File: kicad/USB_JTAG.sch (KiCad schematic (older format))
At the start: 19 parts, among them J1 USB_B, U4 NFM18PS, U5 WE-TVS-824011, U6 FT2232D, U7 6MHz_Crystal, U8 AT93C46DN-SH

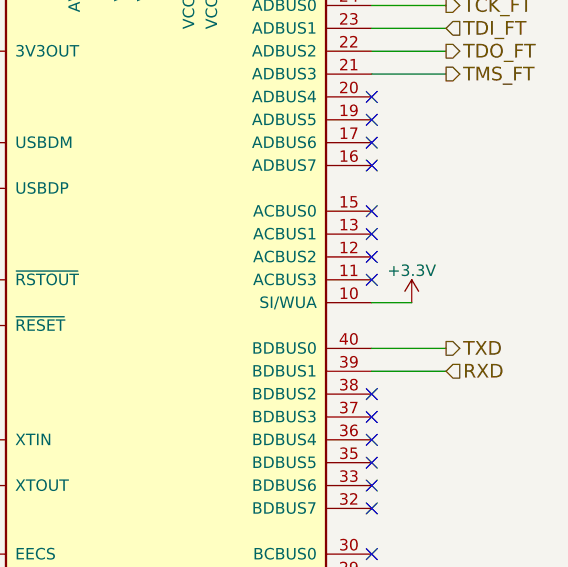
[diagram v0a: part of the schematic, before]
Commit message: Small layout and schematic changes
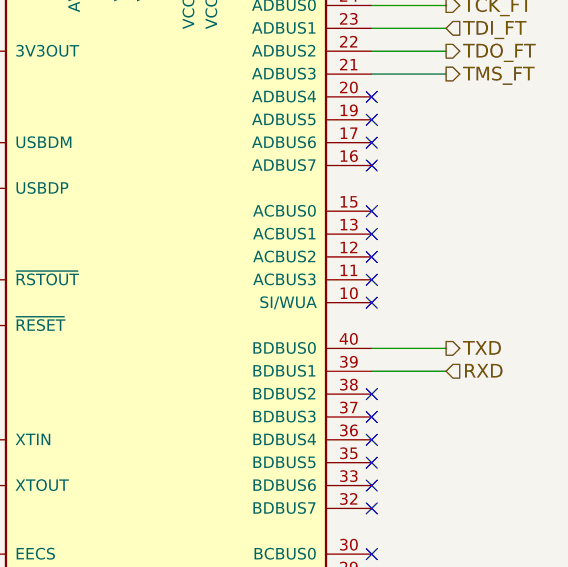
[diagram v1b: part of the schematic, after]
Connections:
- net +3V3: no longer U6.10 (SI/WUA)
- no-connect marks 21 -> 22
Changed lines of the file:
@@
 EESchema Schematic File Version 2
+LIBS:FrequnecyCounter-rescue
 LIBS:power
 LIBS:device
@@
 	1    0    0    -1
 $EndComp
-Wire Wire Line
-	7175 3525 7350 3525
-$Comp
-L +3.3V #PWR044
-U 1 1 59BBED1D
-P 7350 3525
-F 0 "#PWR044" H 7350 3375 50  0001 C CNN
-F 1 "+3.3V" H 7350 3665 50  0000 C CNN
-F 2 "" H 7350 3525 50  0001 C CNN
-F 3 "" H 7350 3525 50  0001 C CNN
-	1    7350 3525
-	1    0    0    -1
-$EndComp
 NoConn ~ 7175 4825
 NoConn ~ 7175 4925
@@
 	1    0    0    -1
 $EndComp
+NoConn ~ 7175 3525
 $EndSCHEMATC

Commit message: Small schematic and layout changes
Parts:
- added Q1: BC846B, TO_SOT_Packages_SMD:SOT-23, symbol BC846B
- added R12: 1k, Resistors_SMD:R_0603_HandSoldering, symbol R
- added R13: 150k, Resistors_SMD:R_0603_HandSoldering, symbol R
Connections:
- net +3V3: now also U6.10 (SI/WUA), U8.6 (ORG), U8.8 (VCC), R12.2
- net +5V: now also U6.4 (~RESET)
- net GND: now also U8.5 (GND), Q1.2 (E)
- net ~RESET: now also Q1.3 (C), R12.1; no longer U6.4 (~RESET)
- net at U6.41 (~PWREN): now also R13.2
- new net: Q1.1 (B), R13.1
- no-connect marks 22 -> 20
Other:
- moved on the sheet: C42
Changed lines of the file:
@@
 $EndComp
 $Comp
-L GND #PWR027
+L GND #PWR025
 U 1 1 595D2BC3
 P 1400 3350
-F 0 "#PWR027" H 1400 3100 50  0001 C CNN
+F 0 "#PWR025" H 1400 3100 50  0001 C CNN
 F 1 "GND" H 1400 3200 50  0000 C CNN
 F 2 "" H 1400 3350 50  0001 C CNN
@@
 $EndComp
 $Comp
-L GND #PWR028
+L GND #PWR026
 U 1 1 595D2BF4
 P 5975 5550
-F 0 "#PWR028" H 5975 5300 50  0001 C CNN
+F 0 "#PWR026" H 5975 5300 50  0001 C CNN
 F 1 "GND" H 5975 5400 50  0000 C CNN
 F 2 "" H 5975 5550 50  0001 C CNN
@@
 $EndComp
 $Comp
-L GND #PWR029
+L GND #PWR027
 U 1 1 595D2BFA
 P 5375 5025
-F 0 "#PWR029" H 5375 4775 50  0001 C CNN
+F 0 "#PWR027" H 5375 4775 50  0001 C CNN
 F 1 "GND" H 5375 4875 50  0000 C CNN
 F 2 "" H 5375 5025 50  0001 C CNN
@@
 $EndComp
 $Comp
-L GND #PWR030
+L GND #PWR028
 U 1 1 595D2C07
 P 5075 2425
-F 0 "#PWR030" H 5075 2175 50  0001 C CNN
+F 0 "#PWR028" H 5075 2175 50  0001 C CNN
 F 1 "GND" H 5075 2275 50  0000 C CNN
 F 2 "" H 5075 2425 50  0001 C CNN
@@
 $EndComp
 $Comp
-L GND #PWR031
+L GND #PWR029
 U 1 1 595D2C1A
 P 5450 2025
-F 0 "#PWR031" H 5450 1775 50  0001 C CNN
+F 0 "#PWR029" H 5450 1775 50  0001 C CNN
 F 1 "GND" H 5450 1875 50  0000 C CNN
 F 2 "" H 5450 2025 50  0001 C CNN
@@
 NoConn ~ 7175 4625
 NoConn ~ 7175 4725
-NoConn ~ 7175 5225
 $Comp
 L AT93C46DN-SH U8
@@
 $EndComp
 $Comp
-L +3.3V #PWR032
+L +3.3V #PWR030
 U 1 1 595E0732
 P 6375 1825
-F 0 "#PWR032" H 6375 1675 50  0001 C CNN
+F 0 "#PWR030" H 6375 1675 50  0001 C CNN
 F 1 "+3.3V" H 6375 1965 50  0000 C CNN
 F 2 "" H 6375 1825 50  0001 C CNN
@@
 $EndComp
 $Comp
-L GND #PWR033
+L GND #PWR031
 U 1 1 595E26E9
 P 2800 2450
-F 0 "#PWR033" H 2800 2200 50  0001 C CNN
+F 0 "#PWR031" H 2800 2200 50  0001 C CNN
 F 1 "GND" H 2800 2300 50  0000 C CNN
 F 2 "" H 2800 2450 50  0001 C CNN
@@
 $EndComp
 $Comp
-L GND #PWR034
+L GND #PWR032
 U 1 1 595E2C1D
 P 2075 3400
-F 0 "#PWR034" H 2075 3150 50  0001 C CNN
+F 0 "#PWR032" H 2075 3150 50  0001 C CNN
 F 1 "GND" H 2075 3250 50  0000 C CNN
 F 2 "" H 2075 3400 50  0001 C CNN
@@
 $EndComp
 $Comp
-L GND #PWR035
+L GND #PWR033
 U 1 1 595E6BEC
 P 2200 2250
-F 0 "#PWR035" H 2200 2000 50  0001 C CNN
+F 0 "#PWR033" H 2200 2000 50  0001 C CNN
 F 1 "GND" H 2200 2100 50  0000 C CNN
 F 2 "" H 2200 2250 50  0001 C CNN
@@
 	1    0    0    -1
 $EndComp
-NoConn ~ 3025 4900
 $Comp
 L C C39
@@
 $EndComp
 $Comp
-L GND #PWR036
+L GND #PWR034
 U 1 1 5961A2DE
 P 2400 3400
-F 0 "#PWR036" H 2400 3150 50  0001 C CNN
+F 0 "#PWR034" H 2400 3150 50  0001 C CNN
 F 1 "GND" H 2400 3250 50  0000 C CNN
 F 2 "" H 2400 3400 50  0001 C CNN
@@
 Text HLabel 7500 2525 2    60   Output ~ 0
 TMS_FT
-Text HLabel 5050 3625 0    60   Input ~ 0
-~RESET
-$Comp
-L +3.3V #PWR037
+$Comp
+L +3.3V #PWR035
 U 1 1 5964E324
 P 3850 4225
-F 0 "#PWR037" H 3850 4075 50  0001 C CNN
+F 0 "#PWR035" H 3850 4075 50  0001 C CNN
 F 1 "+3.3V" H 3850 4365 50  0000 C CNN
 F 2 "" H 3850 4225 50  0001 C CNN
@@
 $EndComp
 $Comp
-L +3.3V #PWR038
+L +3.3V #PWR036
 U 1 1 5964E7A5
-P 2750 4650
-F 0 "#PWR038" H 2750 4500 50  0001 C CNN
-F 1 "+3.3V" H 2750 4790 50  0000 C CNN
-F 2 "" H 2750 4650 50  0001 C CNN
-F 3 "" H 2750 4650 50  0001 C CNN
-	1    2750 4650
+P 2750 4625
+F 0 "#PWR036" H 2750 4475 50  0001 C CNN
+F 1 "+3.3V" H 2750 4765 50  0000 C CNN
+F 2 "" H 2750 4625 50  0001 C CNN
+F 3 "" H 2750 4625 50  0001 C CNN
+	1    2750 4625
 	1    0    0    -1
 $EndComp
@@
 L C C42
 U 1 1 5964E7E9
-P 2750 4800
-F 0 "C42" H 2775 4900 50  0000 L CNN
-F 1 "100n" H 2775 4700 50  0000 L CNN
-F 2 "Capacitors_SMD:C_0603_HandSoldering" H 2788 4650 50  0001 C CNN
-F 3 "" H 2750 4800 50  0001 C CNN
-	1    2750 4800
-	1    0    0    -1
-$EndComp
-$Comp
-L GND #PWR039
+P 2750 4775
+F 0 "C42" H 2775 4875 50  0000 L CNN
+F 1 "100n" H 2775 4675 50  0000 L CNN
+F 2 "Capacitors_SMD:C_0603_HandSoldering" H 2788 4625 50  0001 C CNN
+F 3 "" H 2750 4775 50  0001 C CNN
+	1    2750 4775
+	1    0    0    -1
+$EndComp
+$Comp
+L GND #PWR037
 U 1 1 5964E8AB
-P 2750 4950
-F 0 "#PWR039" H 2750 4700 50  0001 C CNN
-F 1 "GND" H 2750 4800 50  0000 C CNN
-F 2 "" H 2750 4950 50  0001 C CNN
-F 3 "" H 2750 4950 50  0001 C CNN
-	1    2750 4950
-	1    0    0    -1
-$EndComp
-$Comp
-L +5V #PWR040
+P 2750 4925
+F 0 "#PWR037" H 2750 4675 50  0001 C CNN
+F 1 "GND" H 2750 4775 50  0000 C CNN
+F 2 "" H 2750 4925 50  0001 C CNN
+F 3 "" H 2750 4925 50  0001 C CNN
+	1    2750 4925
+	1    0    0    -1
+$EndComp
+$Comp
+L +5V #PWR038
 U 1 1 5968BBC0
 P 2075 1925
-F 0 "#PWR040" H 2075 1775 50  0001 C CNN
+F 0 "#PWR038" H 2075 1775 50  0001 C CNN
 F 1 "+5V" H 2075 2065 50  0000 C CNN
 F 2 "" H 2075 1925 50  0001 C CNN
@@
 $EndComp
 $Comp
-L +5V #PWR041
+L +5V #PWR039
 U 1 1 596B00B1
 P 6125 1700
-F 0 "#PWR041" H 6125 1550 50  0001 C CNN
+F 0 "#PWR039" H 6125 1550 50  0001 C CNN
 F 1 "+5V" H 6125 1840 50  0000 C CNN
 F 2 "" H 6125 1700 50  0001 C CNN
@@
 $EndComp
 $Comp
-L +5V #PWR042
+L +5V #PWR040
 U 1 1 596CAD7A
 P 4950 1675
-F 0 "#PWR042" H 4950 1525 50  0001 C CNN
+F 0 "#PWR040" H 4950 1525 50  0001 C CNN
 F 1 "+5V" H 4950 1815 50  0000 C CNN
 F 2 "" H 4950 1675 50  0001 C CNN
@@
 	6075 1700 6175 1700
 Wire Wire Line
-	2750 4650 3025 4650
+	2750 4625 3025 4625
 Wire Wire Line
 	5375 3625 5050 3625
@@
 Connection ~ 4550 4325
 $Comp
-L GND #PWR043
+L GND #PWR041
 U 1 1 5973DDBE
 P 4550 4350
-F 0 "#PWR043" H 4550 4100 50  0001 C CNN
+F 0 "#PWR041" H 4550 4100 50  0001 C CNN
 F 1 "GND" H 4550 4200 50  0000 C CNN
 F 2 "" H 4550 4350 50  0001 C CNN
@@
 	7175 5025 7300 5025
 $Comp
-L +3.3V #PWR045
+L +3.3V #PWR042
 U 1 1 59C1476A
 P 7300 5025
-F 0 "#PWR045" H 7300 4875 50  0001 C CNN
+F 0 "#PWR042" H 7300 4875 50  0001 C CNN
 F 1 "+3.3V" H 7300 5165 50  0000 C CNN
 F 2 "" H 7300 5025 50  0001 C CNN
@@
 	1    0    0    -1
 $EndComp
-NoConn ~ 7175 3525
+$Comp
+L +5V #PWR043
+U 1 1 59FCA280
+P 5050 3625
+F 0 "#PWR043" H 5050 3475 50  0001 C CNN
+F 1 "+5V" H 5050 3765 50  0000 C CNN
+F 2 "" H 5050 3625 50  0001 C CNN
+F 3 "" H 5050 3625 50  0001 C CNN
+	1    5050 3625
+	1    0    0    -1
+$EndComp
+Wire Wire Line
+	7175 3525 7300 3525
+$Comp
+L +3.3V #PWR044
+U 1 1 59FCF531
+P 7300 3525
+F 0 "#PWR044" H 7300 3375 50  0001 C CNN
+F 1 "+3.3V" H 7300 3665 50  0000 C CNN
+F 2 "" H 7300 3525 50  0001 C CNN
+F 3 "" H 7300 3525 50  0001 C CNN
+	1    7300 3525
+	1    0    0    -1
+$EndComp
+$Comp
+L BC846B Q1
+U 1 1 59FD002C
+P 8100 5225
+F 0 "Q1" H 8300 5300 50  0000 L CNN
+F 1 "BC846B" H 8300 5225 50  0000 L CNN
+F 2 "TO_SOT_Packages_SMD:SOT-23" H 8300 5150 50  0001 L CIN
+F 3 "" H 8100 5225 50  0001 L CNN
+	1    8100 5225
+	1    0    0    -1
+$EndComp
+Wire Wire Line
+	7175 5225 7450 5225
+$Comp
+L R R13
+U 1 1 59FD0390
+P 7600 5225
+F 0 "R13" V 7680 5225 50  0000 C CNN
+F 1 "150k" V 7600 5225 50  0000 C CNN
+F 2 "Resistors_SMD:R_0603_HandSoldering" V 7530 5225 50  0001 C CNN
+F 3 "" H 7600 5225 50  0001 C CNN
+	1    7600 5225
+	0    1    1    0
+$EndComp
+Wire Wire Line
+	7750 5225 7900 5225
+$Comp
+L GND #PWR045
+U 1 1 59FD0919
+P 8200 5475
+F 0 "#PWR045" H 8200 5225 50  0001 C CNN
+F 1 "GND" H 8200 5325 50  0000 C CNN
+F 2 "" H 8200 5475 50  0001 C CNN
+F 3 "" H 8200 5475 50  0001 C CNN
+	1    8200 5475
+	1    0    0    -1
+$EndComp
+Wire Wire Line
+	8200 5475 8200 5425
+$Comp
+L R R12
+U 1 1 59FD09EE
+P 8200 4825
+F 0 "R12" V 8280 4825 50  0000 C CNN
+F 1 "1k" V 8200 4825 50  0000 C CNN
+F 2 "Resistors_SMD:R_0603_HandSoldering" V 8130 4825 50  0001 C CNN
+F 3 "" H 8200 4825 50  0001 C CNN
+	1    8200 4825
+	-1   0    0    1
+$EndComp
+Wire Wire Line
+	8200 4975 8200 5025
+$Comp
+L +3.3V #PWR046
+U 1 1 59FD0CF9
+P 8200 4675
+F 0 "#PWR046" H 8200 4525 50  0001 C CNN
+F 1 "+3.3V" H 8200 4815 50  0000 C CNN
+F 2 "" H 8200 4675 50  0001 C CNN
+F 3 "" H 8200 4675 50  0001 C CNN
+	1    8200 4675
+	1    0    0    -1
+$EndComp
+Wire Wire Line
+	8200 5000 8500 5000
+Connection ~ 8200 5000
+Text HLabel 8500 5000 2    60   Output ~ 0
+~RESET
+Wire Wire Line
+	3025 4625 3025 4725
+NoConn ~ 3025 4825
+$Comp
+L GND #PWR047
+U 1 1 5A0102F0
+P 3025 4925
+F 0 "#PWR047" H 3025 4675 50  0001 C CNN
+F 1 "GND" H 3025 4775 50  0000 C CNN
+F 2 "" H 3025 4925 50  0001 C CNN
+F 3 "" H 3025 4925 50  0001 C CNN
+	1    3025 4925
+	1    0    0    -1
+$EndComp
 $EndSCHEMATC

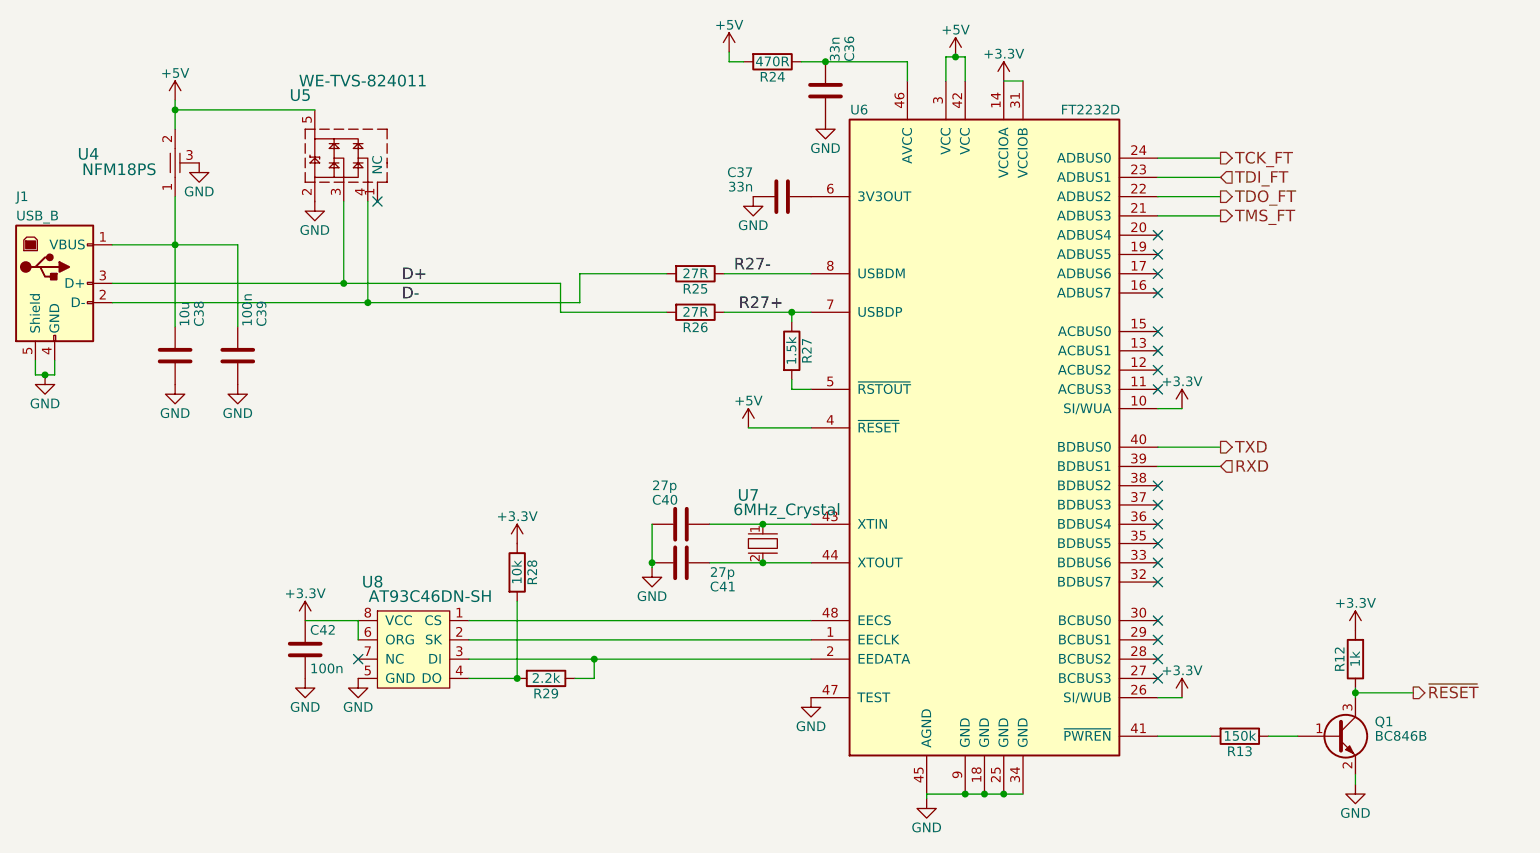
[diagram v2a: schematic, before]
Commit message: Changed some component values to increase the fit & Changed power-supply of the eeprom to use the PWR_EN of the FT2232D
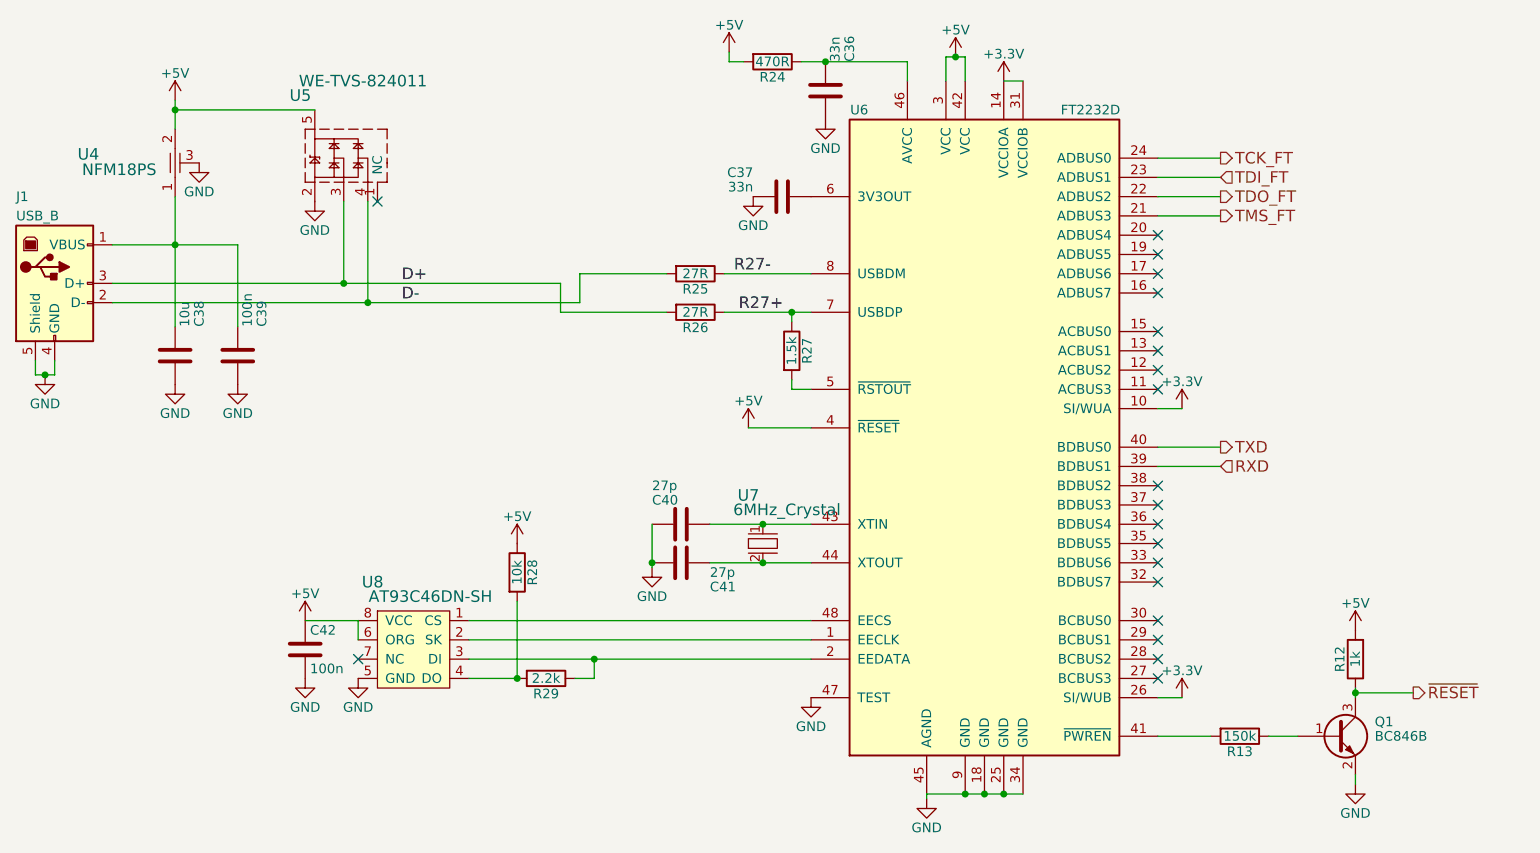
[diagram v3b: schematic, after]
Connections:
- net +3V3: no longer C42.1, R12.2, R28.1, U8.6 (ORG), U8.8 (VCC)
- net +5V: now also C42.1, R12.2, R28.1, U8.6 (ORG), U8.8 (VCC)
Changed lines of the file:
@@
 TMS_FT
-$Comp
-L +3.3V #PWR035
-U 1 1 5964E324
-P 3850 4225
-F 0 "#PWR035" H 3850 4075 50  0001 C CNN
-F 1 "+3.3V" H 3850 4365 50  0000 C CNN
-F 2 "" H 3850 4225 50  0001 C CNN
-F 3 "" H 3850 4225 50  0001 C CNN
-	1    3850 4225
-	1    0    0    -1
-$EndComp
-$Comp
-L +3.3V #PWR036
-U 1 1 5964E7A5
-P 2750 4625
-F 0 "#PWR036" H 2750 4475 50  0001 C CNN
-F 1 "+3.3V" H 2750 4765 50  0000 C CNN
-F 2 "" H 2750 4625 50  0001 C CNN
-F 3 "" H 2750 4625 50  0001 C CNN
-	1    2750 4625
-	1    0    0    -1
-$EndComp
 $Comp
 L C C42
@@
 Wire Wire Line
 	8200 4975 8200 5025
-$Comp
-L +3.3V #PWR046
-U 1 1 59FD0CF9
-P 8200 4675
-F 0 "#PWR046" H 8200 4525 50  0001 C CNN
-F 1 "+3.3V" H 8200 4815 50  0000 C CNN
-F 2 "" H 8200 4675 50  0001 C CNN
-F 3 "" H 8200 4675 50  0001 C CNN
-	1    8200 4675
-	1    0    0    -1
-$EndComp
 Wire Wire Line
 	8200 5000 8500 5000
@@
 	1    0    0    -1
 $EndComp
+$Comp
+L +5V #PWR?
+U 1 1 5A818AEE
+P 2750 4625
+F 0 "#PWR?" H 2750 4475 50  0001 C CNN
+F 1 "+5V" H 2750 4765 50  0000 C CNN
+F 2 "" H 2750 4625 50  0001 C CNN
+F 3 "" H 2750 4625 50  0001 C CNN
+	1    2750 4625
+	1    0    0    -1
+$EndComp
+$Comp
+L +5V #PWR?
+U 1 1 5A818FB4
+P 8200 4675
+F 0 "#PWR?" H 8200 4525 50  0001 C CNN
+F 1 "+5V" H 8200 4815 50  0000 C CNN
+F 2 "" H 8200 4675 50  0001 C CNN
+F 3 "" H 8200 4675 50  0001 C CNN
+	1    8200 4675
+	1    0    0    -1
+$EndComp
+$Comp
+L +5V #PWR?
+U 1 1 5A8195A5
+P 3850 4225
+F 0 "#PWR?" H 3850 4075 50  0001 C CNN
+F 1 "+5V" H 3850 4365 50  0000 C CNN
+F 2 "" H 3850 4225 50  0001 C CNN
+F 3 "" H 3850 4225 50  0001 C CNN
+	1    3850 4225
+	1    0    0    -1
+$EndComp
